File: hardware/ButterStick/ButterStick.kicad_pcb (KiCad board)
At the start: 6 copper layers, 80 x 49 mm, 108 parts, among them CON1 JD1_0001NL, J1 SYZYGY-STD, J2 JST GH Series, J3 SYZYGY-STD, J4 MicroSD, J5 SYZYGY-STD, U1 TLV725P, U10 XCL206, U11 KSZ9031, U12 DAC081C081CIMK, U13 SN74LVC1T45, U14 SN74LVC1T45, U16 TPS73101DBV, U17 DAC081C081CIMK, U18 TPS73101DBV, U19 ATmega328PB-MU, U2 DAC081C081CIMK, U3 ECP5U25, U4 IS66WVH16M8ALL, U5 IS66WVH16M8ALL, U6 MX25R1635, U7 TPS73101DBV, U8 TLV718P, U9 TLV711P, X1 ASDMB, Y1 25Mhz

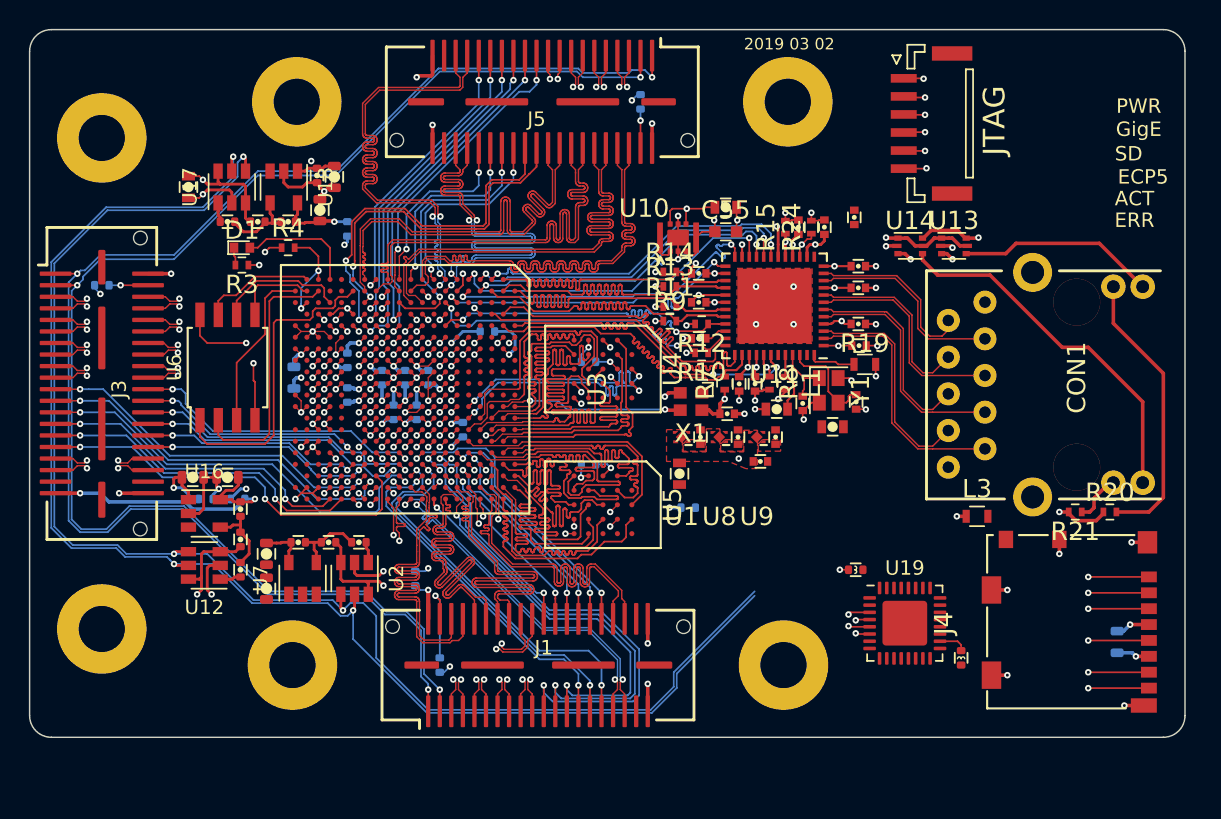
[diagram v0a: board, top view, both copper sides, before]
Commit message: Added ESD on SD card signals.
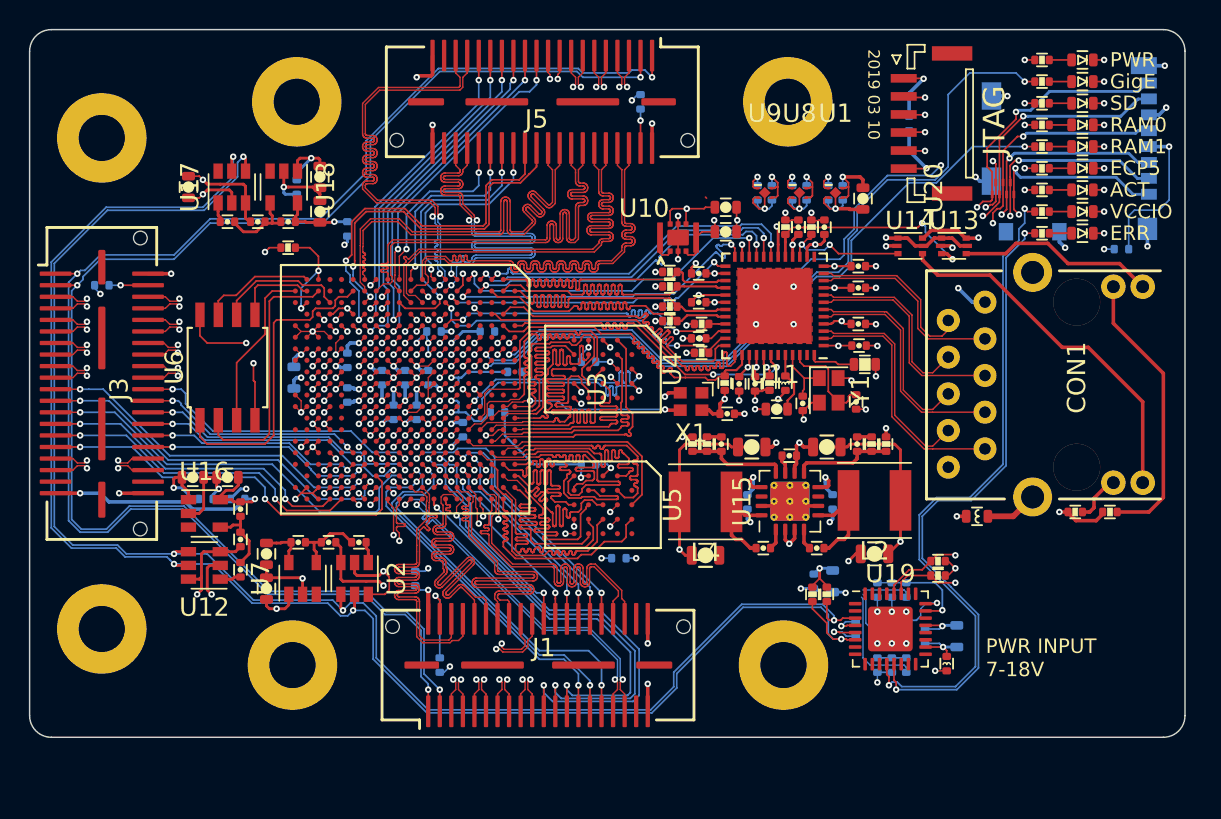
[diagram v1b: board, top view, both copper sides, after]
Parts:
- added C12: 4u7, pkl_dipol:C_0603, B.Cu at (163.1, 119.4)
- added C46: 100n, pkl_dipol:C_0402, B.Cu at (164.7, 122.7)
- added C47: 4u7, pkl_dipol:C_0603, B.Cu at (171.7, 123.2)
- added C50: 100n, pkl_dipol:C_0402, B.Cu at (169.5, 123.2)
- added C51: 1uF, pkl_dipol:C_0402, F.Cu at (160.1, 110.7)
- added C52: 22uF, pkl_dipol:C_0805, F.Cu at (162.7, 110.1)
- added C53: 22uF, pkl_dipol:C_0805, F.Cu at (166.0, 117.5)
- added C54: 22uF, pkl_dipol:C_0805, F.Cu at (157.5, 110.1)
- added C56: 22uF, pkl_dipol:C_0805, F.Cu at (154.3, 117.6)
- added C57: 10pF, pkl_dipol:C_0402, F.Cu at (164.8, 109.9)
- added C58: 10nF, pkl_dipol:C_0402, B.Cu at (163.1, 113.9)
- added C59: 10nF, pkl_dipol:C_0402, B.Cu at (157.2, 113.9)
- added C60: 10pF, pkl_dipol:C_0402, F.Cu at (155.4, 109.9)
- added C61: 10n, pkl_dipol:C_0402, B.Cu at (166.2, 120.0)
- added C62: 10n, pkl_dipol:C_0402, B.Cu at (166.2, 122.6)
- added C63: 10n, pkl_dipol:C_0402, B.Cu at (166.2, 125.2)
- added C64: 100nF, pkl_dipol:C_0402, B.Cu at (163.8, 92.5)
- added C65: 100nF, pkl_dipol:C_0402, B.Cu at (183.1, 96.4)
- added C66: 100nF, pkl_dipol:C_0402, B.Cu at (161.3, 92.5)
- added D2: pkl_LED, pkl_dipol:D_0603, F.Cu at (180.4, 84.8)
- added D3: pkl_LED, pkl_dipol:D_0603, F.Cu at (180.4, 86.3)
- added D4: pkl_LED, pkl_dipol:D_0603, F.Cu at (180.4, 87.8)
- added D5: pkl_LED, pkl_dipol:D_0603, F.Cu at (180.4, 89.3)
- added D6: pkl_LED, pkl_dipol:D_0603, F.Cu at (180.4, 90.8)
- added D7: pkl_LED, pkl_dipol:D_0603, F.Cu at (180.4, 92.3)
- added D8: pkl_LED, pkl_dipol:D_0603, F.Cu at (180.4, 93.8)
- added D9: pkl_LED, pkl_dipol:D_0603, F.Cu at (180.4, 95.3)
- added L2: 2.2uH, Inductor_SMD:L_Taiyo-Yuden_MD-5050, F.Cu at (166.0, 113.8)
- added L4: 2.2uH, Inductor_SMD:L_Taiyo-Yuden_MD-5050, F.Cu at (154.3, 113.9)
- added R27: 2k2, pkl_dipol:R_0402, F.Cu at (161.7, 120.3)
- added R32: 2k2, pkl_dipol:R_0402, F.Cu at (162.7, 120.3)
- added R33: 2k2, pkl_dipol:R_0402, F.Cu at (170.4, 118.0)
- added R34: 2k2, pkl_dipol:R_0402, F.Cu at (170.4, 119.0)
- added R35: 1k, pkl_dipol:R_0402, F.Cu at (177.6, 84.8)
- added R36: 1k, pkl_dipol:R_0402, F.Cu at (177.6, 86.3)
- added R37: 1k, pkl_dipol:R_0402, F.Cu at (177.6, 87.8)
- added R38: 1k, pkl_dipol:R_0402, F.Cu at (177.6, 89.3)
- added R39: 1k, pkl_dipol:R_0402, F.Cu at (177.6, 90.8)
- added R40: 1k, pkl_dipol:R_0402, F.Cu at (177.6, 92.3)
- added R41: 1k, pkl_dipol:R_0402, F.Cu at (177.6, 93.8)
- added R42: 1k, pkl_dipol:R_0402, F.Cu at (177.6, 95.3)
- added R43: 124k, pkl_dipol:R_0402, F.Cu at (165.8, 109.9)
- added R44: 22.1k, pkl_dipol:R_0402, F.Cu at (166.8, 109.9)
- added R45: 73.2k, pkl_dipol:R_0402, F.Cu at (154.4, 109.9)
- added R46: 22.1k, pkl_dipol:R_0402, F.Cu at (153.4, 109.9)
- added R47: 2k2, pkl_dipol:R_0402, B.Cu at (168.2, 120.0)
- added R48: 2k2, pkl_dipol:R_0402, B.Cu at (167.2, 120.0)
- added R49: 2k2, pkl_dipol:R_0402, B.Cu at (168.2, 122.6)
- added R50: 2k2, pkl_dipol:R_0402, B.Cu at (167.2, 122.6)
- added R51: 2k2, pkl_dipol:R_0402, B.Cu at (168.2, 125.2)
- added R52: 2k2, pkl_dipol:R_0402, B.Cu at (167.2, 125.2)
- added R53: 0R, pkl_dipol:R_0402, B.Cu at (135.5, 102.1)
- added R54: 0R, pkl_dipol:R_0402, B.Cu at (139.9, 107.7)
- added R55: 0R, pkl_dipol:R_0402, B.Cu at (141.1, 104.9)
- added U15: TPS542951, Package_DFN_QFN:QFN-16-1EP_4x4mm_P0.65mm_EP2.7x2.7mm_ThermalVias, F.Cu at (160.1, 113.9)
- added U20: PUSB3FR6, gkl_housings_son:XSON7, F.Cu at (174.9, 92.2)
- C11: moved to F.Cu
- C22, C23, C3, C4, C44, C5, FB1: moved to B.Cu
- C48: value 4.7uF -> 100nF; footprint pkl_dipol:C_0603 -> pkl_dipol:C_0402
- C49: value 10uF -> 100nF; footprint pkl_dipol:C_0603 -> pkl_dipol:C_0402
- C55: footprint Capacitors_SMD:C_0603 -> pkl_dipol:C_0603
- D1: value LED -> pkl_LED; footprint LEDs:LED_0402 -> pkl_dipol:D_0603
- J4: footprint bosonFrameGrabber:1040310811 -> gkl_conn:molex_microsd_1040310811; moved to B.Cu
- L1: footprint Inductors_SMD:L_0402 -> pkl_dipol:L_0402
- L3: footprint Inductors_SMD:L_0603 -> pkl_dipol:L_0603
- R10, R11, R12, R13, R14, R15, R20, R21, R24, R3, R4, R7, R8, R9: footprint Resistors_SMD:R_0402 -> pkl_dipol:R_0402
- R19: footprint Resistors_SMD:R_0603 -> pkl_dipol:R_0603
- moved D1 59.6 mm to (180.4, 83.3), turned to 180 degrees
- moved R3 57.2 mm to (177.6, 83.3), turned to 0 degrees
- moved C11 35.4 mm to (165.2, 92.9)
- moved J4 32.7 mm to (185.0, 89.5), turned to 270 degrees
- moved U1 20.0 mm to (163.3, 92.5), turned to 0 degrees
- moved C3 19.1 mm to (162.8, 92.5), turned to 270 degrees
- moved C22 18.6 mm to (158.9, 92.5), turned to 270 degrees
- moved U8 17.8 mm to (160.8, 92.5), turned to 0 degrees
- moved C4 17.3 mm to (160.3, 92.5), turned to 270 degrees
- moved C5 17.0 mm to (157.9, 92.5), turned to 270 degrees
- moved U9 16.9 mm to (158.4, 92.5), turned to 0 degrees
- moved C48 8.47 mm to (162.0, 117.1), turned to 0 degrees
- moved C49 7.76 mm to (158.3, 117.1), turned to 180 degrees
- moved C23 7.53 mm to (168.4, 87.7)
- moved R31 5.94 mm to (148.3, 117.8)
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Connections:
- net Net-(FB1-Pad1) renamed /SmartVIO/VCC
- net Net-(FB2-Pad1) renamed /SmartVIO/AVCC
- net PCLKC6_1 renamed PCLKC1_1
- net PCLKT6_0 renamed PCLKT1_0
- net PCLKT6_1 renamed PCLKT1_1
- net VCCIO0 renamed /sheetFPGA/VCCIO0
- net VCCIO1 renamed /sheetFPGA/VCCIO1
- net VCCIO7 renamed /sheetFPGA/VCCIO7
- C48 pad 1: +5V -> Net-(C48-Pad1)
- C48 pad 2: GND -> Net-(C48-Pad2)
- C49 pad 1: +3V3 -> Net-(C49-Pad1)
- C49 pad 2: GND -> Net-(C49-Pad2)
- J1 pad 1: /SyzygyPort0/syzygySCL -> /SmartVIO/SYZYGY_SCL
- J1 pad 3: /SyzygyPort0/syzygySDA -> /SmartVIO/SYZYGY_SDA
- J3 pad 1: /SyzygyPort0/syzygySCL -> /SmartVIO/SYZYGY_SCL
- J3 pad 3: /SyzygyPort0/syzygySDA -> /SmartVIO/SYZYGY_SDA
- J5 pad 1: /SyzygyPort0/syzygySCL -> /SmartVIO/SYZYGY_SCL
- J5 pad 3: /SyzygyPort0/syzygySDA -> /SmartVIO/SYZYGY_SDA
- R3 pad 1: GND -> +3V3
- R3 pad 2: Net-(D1-Pad1) -> Net-(D1-PadA)
- U12 pad 4: /SyzygyPort0/pmicSDA -> /SmartVIO/PMIC_SDA
- U12 pad 5: /SyzygyPort0/pmicSCL -> /SmartVIO/PMIC_SCL
- U17 pad 4: /SyzygyPort0/pmicSDA -> /SmartVIO/PMIC_SDA
- U17 pad 5: /SyzygyPort0/pmicSCL -> /SmartVIO/PMIC_SCL
- U17 pad 6: GND -> /SyzygyPort2/sheet5C8EBAFC/PMIC_ADR0
- U19 pad 12: Net-(U19-Pad12) -> LED_VCCIO
- U19 pad 13: Net-(U19-Pad13) -> LED_ERR
- U19 pad 27: /SmartVIO/SDA0 -> /SmartVIO/SYZYGY_SDA
- U19 pad 28: /SmartVIO/SCL0 -> /SmartVIO/SYZYGY_SCL
- U19 pad 3: /SmartVIO/SDA1 -> /SmartVIO/PMIC_SDA
- U19 pad 6: /SmartVIO/SCL1 -> /SmartVIO/PMIC_SCL
- U2 pad 4: /SyzygyPort0/pmicSDA -> /SmartVIO/PMIC_SDA
- U2 pad 5: /SyzygyPort0/pmicSCL -> /SmartVIO/PMIC_SCL
- U2 pad 6: GND -> +3V3
- U3 pad A7: Net-(U3-PadA7) -> LED_ACT
- U3 pad B6: SD_CMD -> SD_DAT0
- U3 pad C7: Net-(U3-PadC7) -> LED_GigE
- U3 pad C8: Net-(U3-PadC8) -> LED_RAM1
- U3 pad D6: SD_DAT3 -> SD_DAT1
- U3 pad D7: SD_DAT1 -> SD_DAT2
- U3 pad D8: Net-(U3-PadD8) -> LED_RAM0
- U3 pad E6: SD_DAT2 -> SD_CMD
- U3 pad E7: SD_DAT0 -> SD_DAT3
- U3 pad E8: Net-(U3-PadE8) -> LED_SD
- U3 pad U1: LED_A -> Net-(U3-PadU1)
- U3 pad Y3: FPGA_CDONE -> LED_ECP5
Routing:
- net /SmartVIO/SYZYGY_SCL: track 0.00 -> 154.7 mm, vias 0 -> 4
- net /SmartVIO/SYZYGY_SDA: track 0.00 -> 150.6 mm, vias 0 -> 4
- net /SmartVIO/PMIC_SCL: track 0.00 -> 110.1 mm, vias 0 -> 4
- net /SmartVIO/PMIC_SDA: track 0.00 -> 107.1 mm, vias 0 -> 4
- net /SyzygyPort0/syzygySCL: track 101.1 -> 0.00 mm, vias 3 -> 0
- net /SyzygyPort0/syzygySDA: track 99.8 -> 0.00 mm, vias 3 -> 0
- net /SyzygyPort0/pmicSDA: track 98.1 -> 0.00 mm, vias 3 -> 0
- net /SyzygyPort0/pmicSCL: track 97.5 -> 0.00 mm, vias 3 -> 0
- net LED_SD: track 0.00 -> 57.8 mm, vias 0 -> 2
- net GND: track 165.0 -> 220.5 mm, vias 129 -> 162
- net LED_RAM0: track 0.00 -> 54.7 mm, vias 0 -> 2
- net LED_GigE: track 0.00 -> 53.6 mm, vias 0 -> 2
- net LED_RAM1: track 0.00 -> 47.5 mm, vias 0 -> 2
- net LED_ACT: track 0.00 -> 47.4 mm, vias 0 -> 3
- net LED_VCCIO: track 0.00 -> 46.8 mm, vias 0 -> 2
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- added copper zone on In3.Cu, net VCCIO0
- added copper zone on In3.Cu, net VCCIO1
- added copper zone on In3.Cu, net VCCIO7
- removed copper zone on F.Cu, net +1V1
- removed copper zone on F.Cu, net +1V8
- removed copper zone on F.Cu, net +2V5
- removed copper zone on F.Cu, net +3V3
- removed copper zone on In3.Cu, net /sheetFPGA/VCCIO0
- removed copper zone on In3.Cu, net /sheetFPGA/VCCIO1
- removed copper zone on In3.Cu, net /sheetFPGA/VCCIO7
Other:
- rule solder_mask_min_width: 0.25 -> 0.1
- board text added: "2019 03 10"
- board text added: "PWR INPUT 7-18V"
- board text added: "RAM0"
- board text added: "RAM1"
- board text added: "VCCIO"
- board text removed: "2019 03 02"

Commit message: Finished initial routing of PCB.. Most parts are finished.
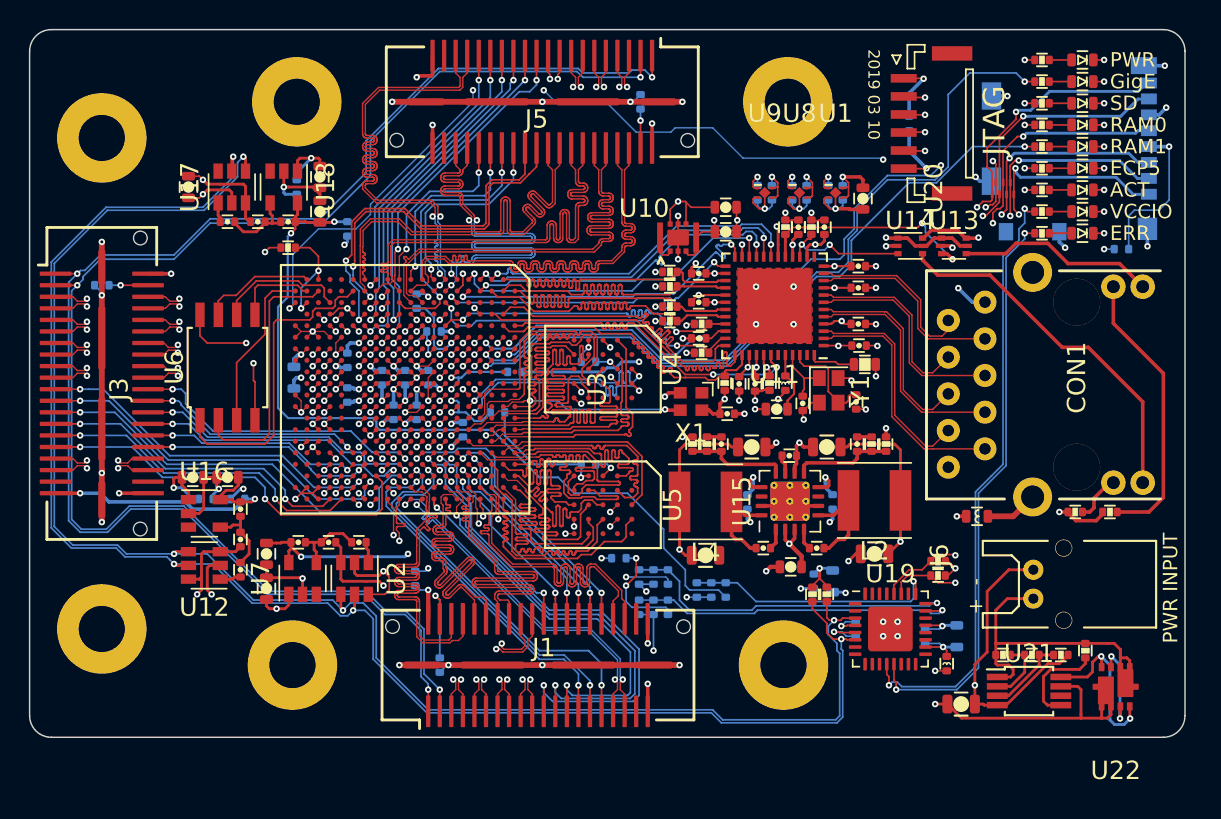
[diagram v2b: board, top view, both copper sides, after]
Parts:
- added C67: 10uF, pkl_dipol:C_0805, F.Cu at (172.0, 127.9)
- added C68: 100n, pkl_dipol:C_0603, F.Cu at (160.2, 118.4)
- added J6: JST_PA, gkl_conn:SB02B-PASK-2, F.Cu at (177.0, 119.6)
- added R56: 124k, pkl_dipol:R_0402, F.Cu at (174.9, 124.5)
- added R57: 124k, pkl_dipol:R_0402, F.Cu at (176.9, 124.5)
- added R58: 124k, pkl_dipol:R_0402, F.Cu at (178.9, 124.5)
- added R59: 510k, pkl_dipol:R_0402, F.Cu at (180.6, 124.2)
- added U21: LTC4367, Package_SO:MSOP-8_3x3mm_P0.65mm, F.Cu at (176.7, 127.0)
- added U22: AON7804, gkl_housings_dfn:DFN3X3_8L_EP2_P, F.Cu at (182.7, 126.7)
- moved C62 16.9 mm to (149.7, 119.1)
- moved R49 16.9 mm to (151.7, 119.1)
- moved R50 16.9 mm to (150.7, 119.1)
- moved C61 16.5 mm to (149.7, 121.2)
- moved R47 16.5 mm to (151.7, 121.2)
- moved R48 16.5 mm to (150.7, 121.2)
- moved C63 13.5 mm to (153.7, 120.0)
- moved R51 13.5 mm to (155.7, 120.0)
- moved R52 13.5 mm to (154.7, 120.0)
- moved C20 5.33 mm to (134.3, 100.0), turned to 90 degrees
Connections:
- J1 pad 41: (no net) -> GND
- J3 pad 41: (no net) -> GND
- J5 pad 41: (no net) -> GND
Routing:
- net GND: track 220.5 -> 303.6 mm, vias 162 -> 173
- net LED_ECP5: track 0.70 -> 64.2 mm, vias 1 -> 5
- net Net-(C67-Pad1): track 2.23 -> 51.0 mm, vias 1 -> 2
- net /sheetFPGA/PORT2_VCCIO: track 28.7 -> 72.3 mm, vias 2 -> 3
- net +2V5: track 37.6 -> 72.2 mm
- net +1V1: track 20.1 -> 53.1 mm
- net /sheetFPGA/PORT0_VCCIO: track 19.1 -> 47.7 mm, vias 2 -> 5
- net /sheetFPGA/PORT1_VCCIO: track 24.9 -> 52.9 mm, vias 2 -> 3
- net Net-(J6-Pad1): track 0.00 -> 23.2 mm
- net +1V8: track 104.1 -> 123.7 mm, vias 17 -> 18
- net /SmartVIO/ADC_1: track 5.73 -> 23.6 mm
- net /SmartVIO/ADC_2: track 2.00 -> 17.7 mm, vias 0 -> 1
- net /SmartVIO/ADC_0: track 7.29 -> 22.8 mm
- net +5V: track 161.0 -> 175.3 mm
- net Net-(U21-Pad8): track 0.00 -> 11.7 mm, vias 0 -> 2
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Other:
- board text added: "+ -"
- board text added: "PWR INPUT"
- board text removed: "PWR INPUT 7-18V"

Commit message: Update KiCad PCB.
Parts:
- added C69: 10uF, pkl_dipol:C_0805, F.Cu at (157.8, 118.6)
- added C70: 10uF, pkl_dipol:C_0805, F.Cu at (162.5, 118.6)
- added C71: 100n, pkl_dipol:C_0402, F.Cu at (171.6, 121.9)
- added G***: LOGO, LOGO, F.Cu at (141.9, 93.7)
- added G***: LOGO, OSHW_basic, F.Cu at (120.0, 86.2)
- added G***: LOGO, Gsd_logo, F.Cu at (120.0, 88.7)
- added J7: TagConnect, pkl_tag_connect:TC2030-NL_SMALL, B.Cu at (170.9, 117.6)
- added R60: 2k2, pkl_dipol:R_0402, F.Cu at (170.4, 117.1)
- added R61: 10k, pkl_dipol:R_0402, B.Cu at (164.5, 111.8)
- added R62: 10k, pkl_dipol:R_0402, B.Cu at (164.5, 110.8)
- added Y2: Resonator, Crystal:Resonator_SMD_muRata_CSTxExxV-3Pin_3.0x1.1mm, F.Cu at (164.9, 127.9)
- moved R55 2.83 mm to (138.3, 105.3)
- moved C68 0.71 mm to (160.1, 119.1), turned to 270 degrees
- moved R27 0.54 mm to (161.9, 120.8)
- moved R32 0.54 mm to (162.9, 120.8)
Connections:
- U15 pad 14: Net-(U15-Pad14) -> /sheetPower/EN2
- U15 pad 7: Net-(U15-Pad7) -> /sheetPower/EN1
- U16 pad 3: /SyzygyPort1/sheet5C8A3B42/EN -> /SyzygyPort1/EN
- U18 pad 3: /SyzygyPort2/sheet5C8EBAFC/EN -> /SyzygyPort2/EN
- U19 pad 10: Net-(U19-Pad10) -> /SyzygyPort1/EN
- U19 pad 11: Net-(U19-Pad11) -> /SyzygyPort2/EN
- U19 pad 15: Net-(U19-Pad15) -> /SmartVIO/MOSI
- U19 pad 16: Net-(U19-Pad16) -> /SmartVIO/MISO
- U19 pad 17: Net-(U19-Pad17) -> /SmartVIO/SCK
- U19 pad 29: Net-(U19-Pad29) -> /SmartVIO/RESET
- U19 pad 9: Net-(U19-Pad9) -> /SyzygyPort0/EN
- U3 pad C6: Net-(U3-PadC6) -> SD_CD
- U7 pad 3: /SyzygyPort0/SyzygyStandard/EN -> /SyzygyPort0/EN
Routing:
- net /SyzygyPort2/EN: track 0.00 -> 106.9 mm, vias 0 -> 2
- net /SyzygyPort1/EN: track 0.00 -> 62.6 mm, vias 0 -> 2
- net +5V: track 175.3 -> 230.1 mm, vias 9 -> 14
- net /SyzygyPort0/EN: track 0.00 -> 45.0 mm, vias 0 -> 2
- net SD_CD: track 0.00 -> 41.5 mm, vias 0 -> 2
- net Net-(C67-Pad1): track 51.0 -> 69.8 mm, vias 2 -> 3
- net LED_VCCIO: track 42.2 -> 59.7 mm
- net LED_ERR: track 40.3 -> 57.6 mm
- net /SmartVIO/MISO: track 0.00 -> 14.1 mm, vias 0 -> 1
- net /SmartVIO/MOSI: track 0.00 -> 13.8 mm, vias 0 -> 1
- net +1V8: track 123.7 -> 110.1 mm, vias 18 -> 16
- net /SmartVIO/RESET: track 0.00 -> 13.0 mm, vias 0 -> 2
- net /SmartVIO/SCK: track 0.00 -> 12.7 mm, vias 0 -> 1
- net +1V2: track 52.3 -> 62.6 mm
- net /sheetPower/EN2: track 0.00 -> 9.79 mm, vias 0 -> 1
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- added copper zone on In3.Cu, net +1V8
- added copper zone on F.Cu, net +3V3
- added copper zone on F.Cu, net +5V
- added copper zone on In3.Cu, net +5V
- added copper zone on In3.Cu, net /SmartVIO/VCC
- added copper zone on In3.Cu, net /sheetFPGA/VCCIO0
- added copper zone on In3.Cu, net /sheetFPGA/VCCIO1
- added copper zone on In3.Cu, net /sheetFPGA/VCCIO7
- added copper zone on F.Cu, net Net-(C48-Pad2)
- added copper zone on F.Cu, net Net-(C49-Pad2)
- added copper zone on F.Cu, net Net-(C67-Pad1)
- removed copper zone on In3.Cu, net VCCIO0
- removed copper zone on In3.Cu, net VCCIO1
- removed copper zone on In3.Cu, net VCCIO7
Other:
- board text added: "2019 03 11"
- board text removed: "2019 03 10"

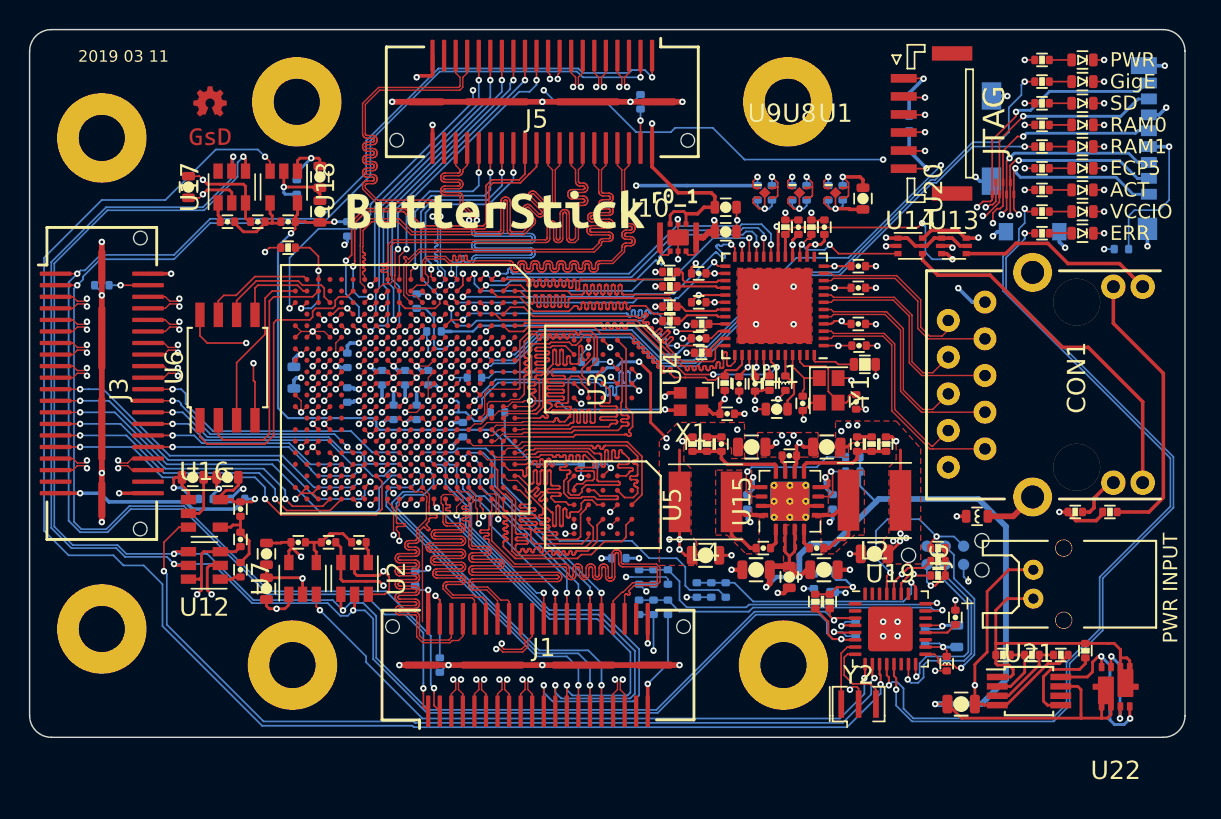
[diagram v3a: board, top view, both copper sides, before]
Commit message: Update two diff-pairs from L6 onto L3. Update Images
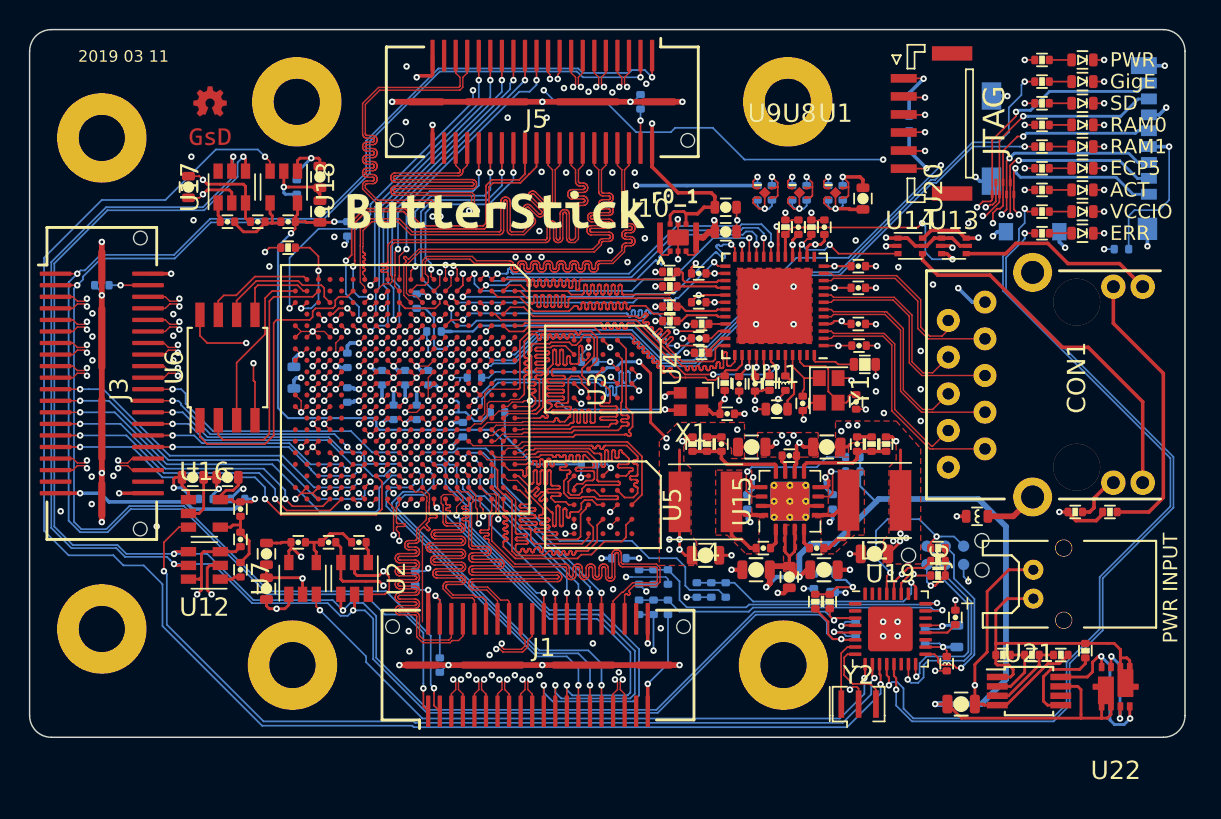
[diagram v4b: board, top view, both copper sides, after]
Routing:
- net /SyzygyPort2/D1_N: track 32.5 -> 30.7 mm
- net GND: vias 180 -> 237
